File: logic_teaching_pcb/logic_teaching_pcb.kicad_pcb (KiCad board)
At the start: 2 copper layers, 200 x 150 mm, 79 parts, among them J1 Conn_01x02, J10 Conn_01x01, J11 Conn_01x01, J12 Conn_01x01, J13 Conn_01x02, J14 Conn_01x01, J15 Conn_01x02, J16 Conn_01x01, J17 Conn_01x01, J18 Conn_01x01, J19 Conn_01x01, J2 Conn_01x02, J20 Conn_01x01, J21 Conn_01x01, J22 Conn_01x01, J23 Conn_01x01, J24 Conn_01x01, J25 Conn_01x02, J26 Conn_01x01, J27 Conn_01x02, J28 Conn_01x01, J29 Conn_01x02, J3 Conn_01x02, J30 Conn_01x02, J31 Conn_01x02, J32 Conn_01x01, J33 Conn_01x02, J34 Conn_01x01, J35 Conn_01x02, J36 Conn_01x01, J37 Conn_01x02, J38 Conn_01x01, J39 Conn_01x02, J4 Conn_01x02, J40 Conn_01x01, J41 Conn_01x02, J42 Conn_01x01, J45 Conn_01x01, J5 Conn_01x01, J59 Conn_01x02, J6 Conn_01x01, J60 Conn_01x02, J61 Conn_01x02, J62 Conn_01x02, J63 Conn_01x01, J64 Conn_01x01, J65 Conn_01x01, J66 Conn_01x01, J7 Conn_01x01, J8 Conn_01x01, J9 Conn_01x01, SW1 SW_SPDT, SW2 SW_SPDT, SW3 SW_SPDT, SW4 SW_SPDT, SW5 SW_Push, U1 74HC00, U2 74HC00

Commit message: finish first PCB draft
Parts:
- added J43: Conn_01x02, Connector_PinHeader_2.54mm:PinHeader_1x02_P2.54mm_Vertical, F.Cu at (233.0, 327.0)
- added J44: Conn_01x01, Connector:Banana_Jack_1Pin, F.Cu at (230.5, 315.0)
- added J46: Conn_01x02, Connector_PinHeader_2.54mm:PinHeader_1x02_P2.54mm_Vertical, F.Cu at (233.0, 365.0)
- added J47: Conn_01x01, Connector:Banana_Jack_1Pin, F.Cu at (230.5, 353.0)
- added J48: Conn_01x02, Connector_PinHeader_2.54mm:PinHeader_1x02_P2.54mm_Vertical, F.Cu at (233.0, 403.0)
- added J49: Conn_01x01, Connector:Banana_Jack_1Pin, F.Cu at (230.5, 391.0)
- added J50: Conn_01x02, Connector_PinHeader_2.54mm:PinHeader_1x02_P2.54mm_Vertical, F.Cu at (188.5, 326.0)
- added J51: Conn_01x01, Connector:Banana_Jack_1Pin, F.Cu at (190.5, 314.0)
- added J52: Conn_01x02, Connector_PinHeader_2.54mm:PinHeader_1x02_P2.54mm_Vertical, F.Cu at (188.5, 364.0)
- added J53: Conn_01x01, Connector:Banana_Jack_1Pin, F.Cu at (190.5, 352.0)
- added J54: Conn_01x02, Connector_PinHeader_2.54mm:PinHeader_1x02_P2.54mm_Vertical, F.Cu at (188.5, 402.0)
- added J55: Conn_01x01, Connector:Banana_Jack_1Pin, F.Cu at (190.5, 390.0)
- added J56: Conn_01x01, Connector_PinHeader_2.54mm:PinHeader_1x01_P2.54mm_Vertical, F.Cu at (196.5, 341.5)
- added J57: Conn_01x01, Connector_PinHeader_2.54mm:PinHeader_1x01_P2.54mm_Vertical, F.Cu at (196.5, 380.0)
- added J58: Conn_01x01, Connector_PinHeader_2.54mm:PinHeader_1x01_P2.54mm_Vertical, F.Cu at (196.5, 418.0)
- added J67: Conn_01x01, Connector_PinHeader_2.54mm:PinHeader_1x01_P2.54mm_Vertical, F.Cu at (81.5, 376.0)
- added J68: Conn_01x01, Connector_PinHeader_2.54mm:PinHeader_1x01_P2.54mm_Vertical, F.Cu at (76.5, 397.0)
- added J69: Conn_01x01, Connector_PinHeader_2.54mm:PinHeader_1x01_P2.54mm_Vertical, F.Cu at (86.5, 397.0)
- added J70: Conn_01x01, Connector:Banana_Jack_1Pin, F.Cu at (85.5, 413.0)
- added R7: 10k, Resistor_SMD:R_1206_3216Metric_Pad1.30x1.75mm_HandSolder, B.Cu at (196.5, 331.0)
- added R8: 10k, Resistor_SMD:R_1206_3216Metric_Pad1.30x1.75mm_HandSolder, B.Cu at (196.5, 369.0)
- added R9: 10k, Resistor_SMD:R_1206_3216Metric_Pad1.30x1.75mm_HandSolder, B.Cu at (196.5, 407.0)
- added SW6: SW_Push, Button_Switch_THT:SW_PUSH-12mm, F.Cu at (204.2, 323.5)
- added SW7: SW_Push, Button_Switch_THT:SW_PUSH-12mm, F.Cu at (204.2, 361.5)
- added SW8: SW_Push, Button_Switch_THT:SW_PUSH-12mm, F.Cu at (204.2, 399.5)
- J10, J12: value Conn_01x01 -> Conn_01x02; footprint Connector_PinHeader_2.54mm:PinHeader_1x01_P2.54mm_Vertical -> Connector_PinHeader_2.54mm:PinHeader_1x02_P2.54mm_Vertical
- J11: footprint Connector_PinHeader_2.54mm:PinHeader_1x01_P2.54mm_Vertical -> Connector:Banana_Jack_1Pin
- R2, R3, R4, R5: moved to B.Cu
- moved J17 534.5 mm to (50.5, 367.0)
- moved J24 522.3 mm to (60.5, 397.0)
- moved J23 517.2 mm to (50.5, 397.0)
- moved J20 503.5 mm to (76.5, 367.0)
- moved J22 494.9 mm to (55.5, 376.0)
- moved J19 489.0 mm to (81.5, 346.0)
- moved J9 488.6 mm to (55.5, 346.0)
- moved J36 487.3 mm to (131.5, 361.0)
- moved J35 485.4 mm to (137.5, 368.5)
- moved J21 479.9 mm to (86.5, 367.0)
- moved J18 479.9 mm to (60.5, 367.0)
- moved SW4 476.1 mm to (92.8, 389.0), turned to 90 degrees
- moved R5 467.7 mm to (142.5, 370.0)
- moved SW3 464.3 mm to (66.8, 389.0), turned to 90 degrees
- moved D8 456.4 mm to (155.5, 370.0), turned to 180 degrees
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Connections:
- J10 pad 1: Net-(J10-Pad1) -> Net-(R1-Pad2)
- J11 pad 1: Net-(J11-Pad1) -> Net-(R1-Pad2)
- J12 pad 1: Net-(J12-Pad1) -> GND
- R1 pad 2: +3V0 -> Net-(R1-Pad2)
- SW2 pad 1: Net-(J19-Pad1) -> Net-(J20-Pad1)
- SW2 pad 2: Net-(J10-Pad1) -> Net-(J19-Pad1)
- SW2 pad 3: Net-(J20-Pad1) -> Net-(J21-Pad1)
- SW3 pad 1: Net-(J21-Pad1) -> Net-(J23-Pad1)
- SW3 pad 2: Net-(J11-Pad1) -> Net-(J22-Pad1)
- SW3 pad 3: Net-(J22-Pad1) -> Net-(J24-Pad1)
- SW4 pad 1: Net-(J23-Pad1) -> Net-(J68-Pad1)
- SW4 pad 2: Net-(J12-Pad1) -> Net-(J67-Pad1)
- SW4 pad 3: Net-(J24-Pad1) -> Net-(J69-Pad1)
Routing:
- net +BATT: track 0.00 -> 274.6 mm
- net Net-(R1-Pad2): track 0.00 -> 56.8 mm
- net Net-(J54-Pad1): track 0.00 -> 48.4 mm
- net Net-(J52-Pad1): track 0.00 -> 48.4 mm
- net Net-(J50-Pad1): track 0.00 -> 48.4 mm
- net Net-(J48-Pad1): track 0.00 -> 42.2 mm
- net Net-(J46-Pad1): track 0.00 -> 42.2 mm
- net Net-(J43-Pad1): track 0.00 -> 42.2 mm
- net Net-(D7-Pad1): track 0.00 -> 29.4 mm
- net Net-(D5-Pad1): track 0.00 -> 29.4 mm
- net Net-(D3-Pad1): track 0.00 -> 29.4 mm
- net Net-(D1-Pad1): track 0.00 -> 29.4 mm
- net Net-(J69-Pad1): track 0.00 -> 23.7 mm
- net Net-(J21-Pad1): track 0.00 -> 23.7 mm
- net Net-(J24-Pad1): track 0.00 -> 23.7 mm
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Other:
- board size 200 x 150 mm -> 200 x 180 mm
- board text added: "Battery"
- board text added: "Buttons"
- board text added: "LEDs"
- board text added: "Logic ICs"
- board text added: "Switches"
- board text added: "V+"
- board text added: "V-"
- board text added: "VBATT"
- board text removed: "Logic Gates"

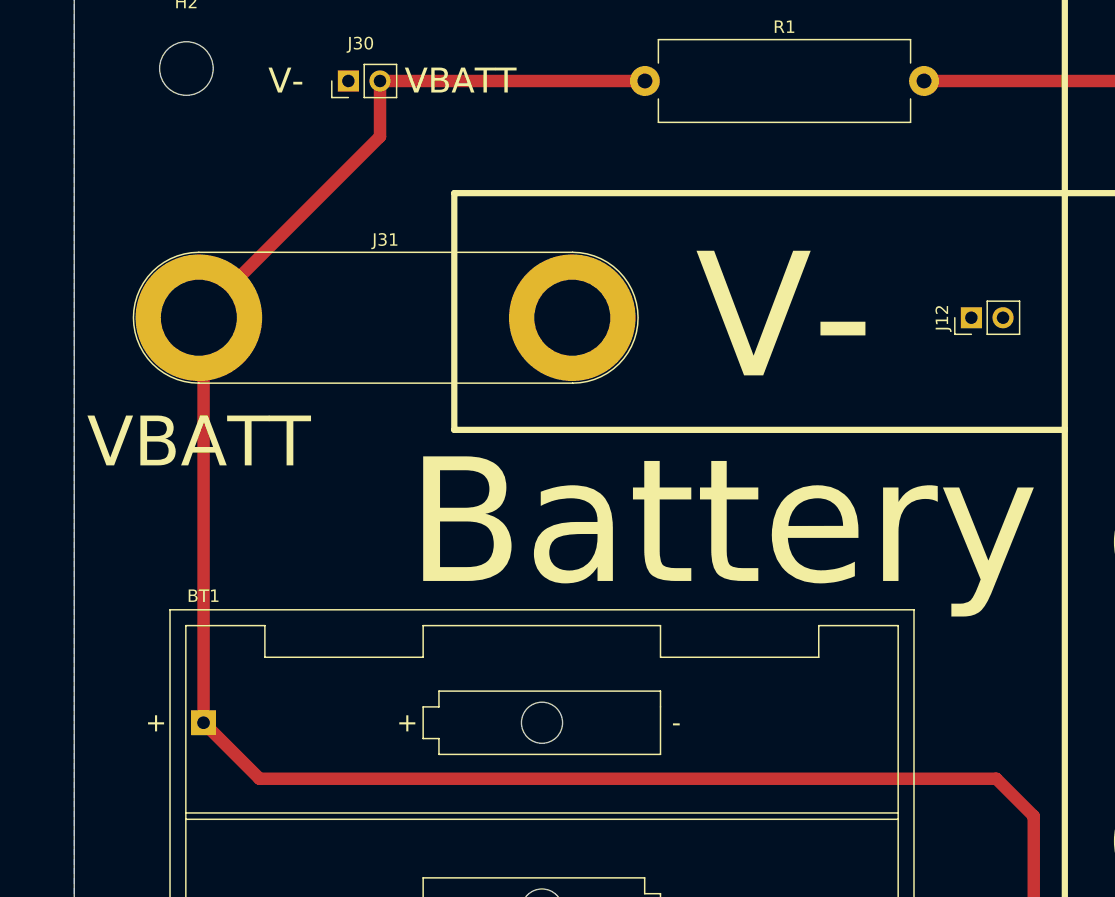
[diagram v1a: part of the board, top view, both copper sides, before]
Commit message: Added power switch
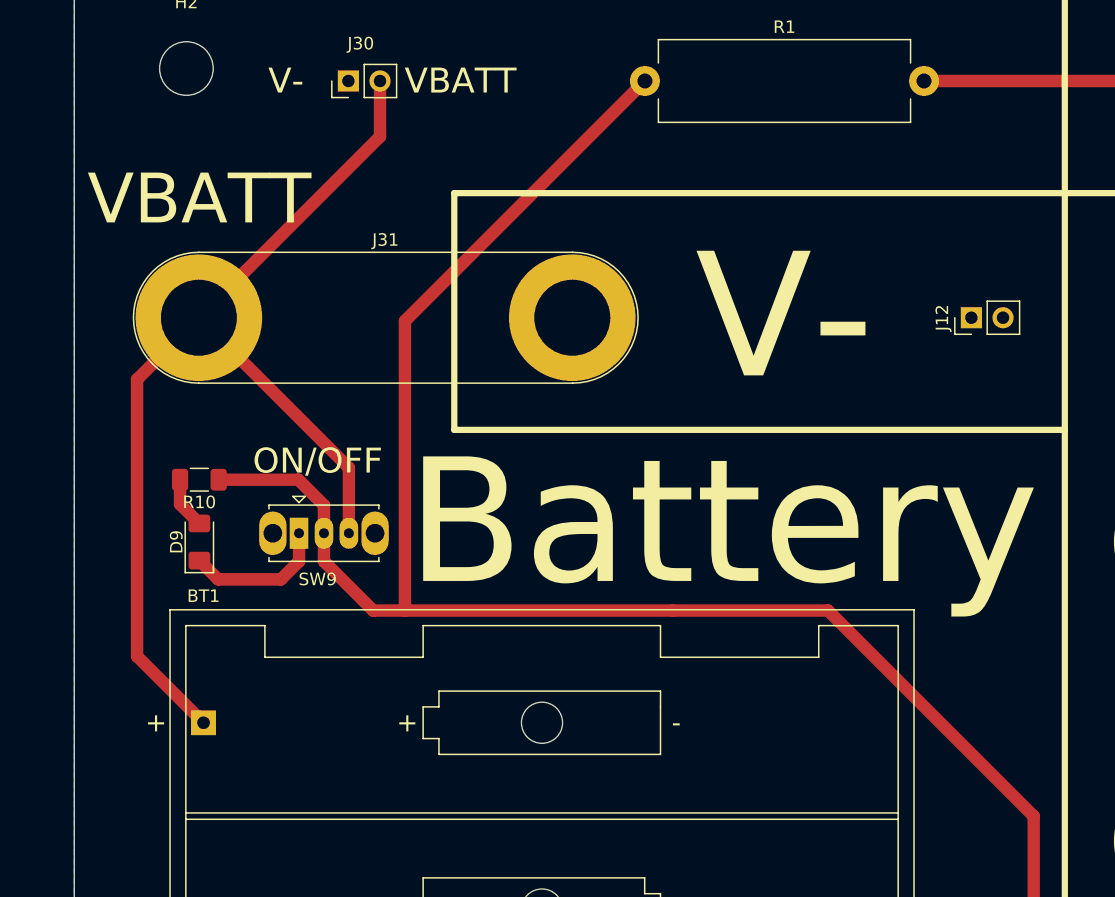
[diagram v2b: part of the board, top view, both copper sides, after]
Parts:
- added D9: LED, LED_SMD:LED_1206_3216Metric_Pad1.42x1.75mm_HandSolder, F.Cu at (52.5, 289.0)
- added R10: 200, Resistor_SMD:R_1206_3216Metric_Pad1.30x1.75mm_HandSolder, F.Cu at (52.5, 284.0)
- added SW9: SW_SPDT, Button_Switch_THT:SW_Slide_1P2T_CK_OS102011MS2Q, F.Cu at (60.5, 288.3)
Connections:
- BT1 pad 1: +BATT -> Net-(BT1-Pad1)
- J30 pad 2: +BATT -> Net-(BT1-Pad1)
- J31 pad 1: +BATT -> Net-(BT1-Pad1)
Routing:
- net Net-(BT1-Pad1): track 0.00 -> 84.1 mm
- net +BATT: track 274.6 -> 255.7 mm
- net GND: track 0.00 -> 11.5 mm
- net Net-(D9-Pad2): track 0.00 -> 4.15 mm
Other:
- board text added: "ON/OFF"
